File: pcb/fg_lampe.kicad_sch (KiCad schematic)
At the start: 42 parts, among them J1 ISP Port, J2 I^{2}C Debug, J3 RX/TX, J4 1792863, J5 1792863, J6 1792863, SW1 Reset Button, U1 ATmega328P-P, U2 L7805, U3 MAX1044, U4 MAX1044, U5 MCP4812, U8 MCP3008, Y1 16MHz

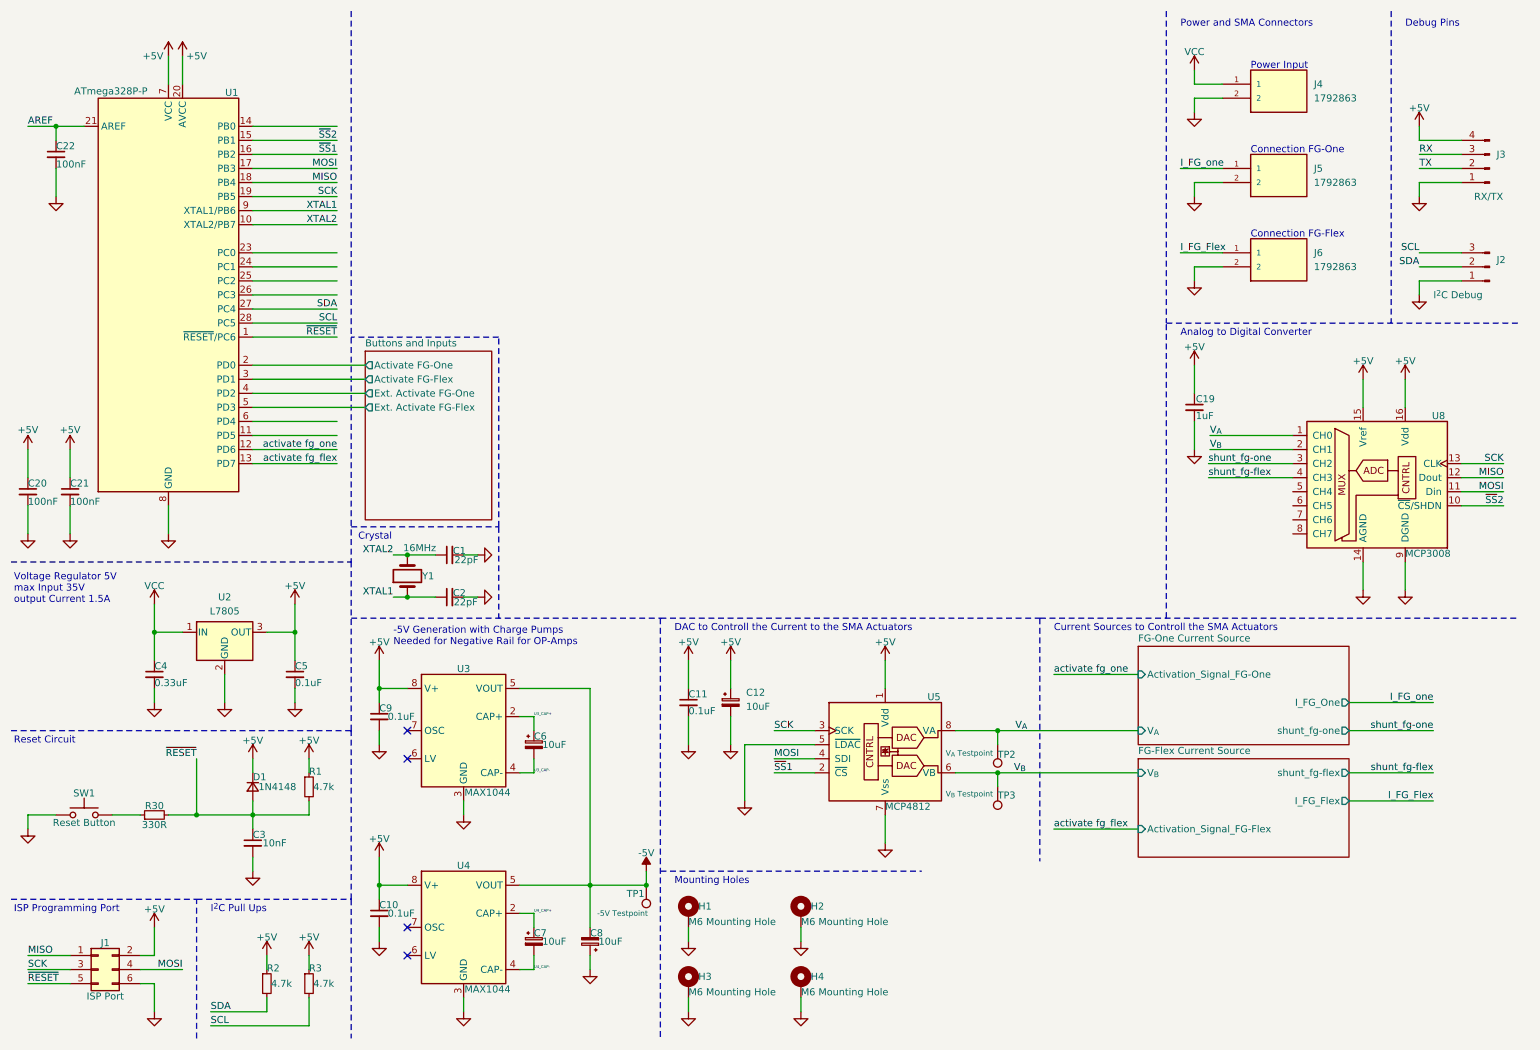
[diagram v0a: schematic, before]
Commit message: potentiometer to set pwm for warm and cold light added
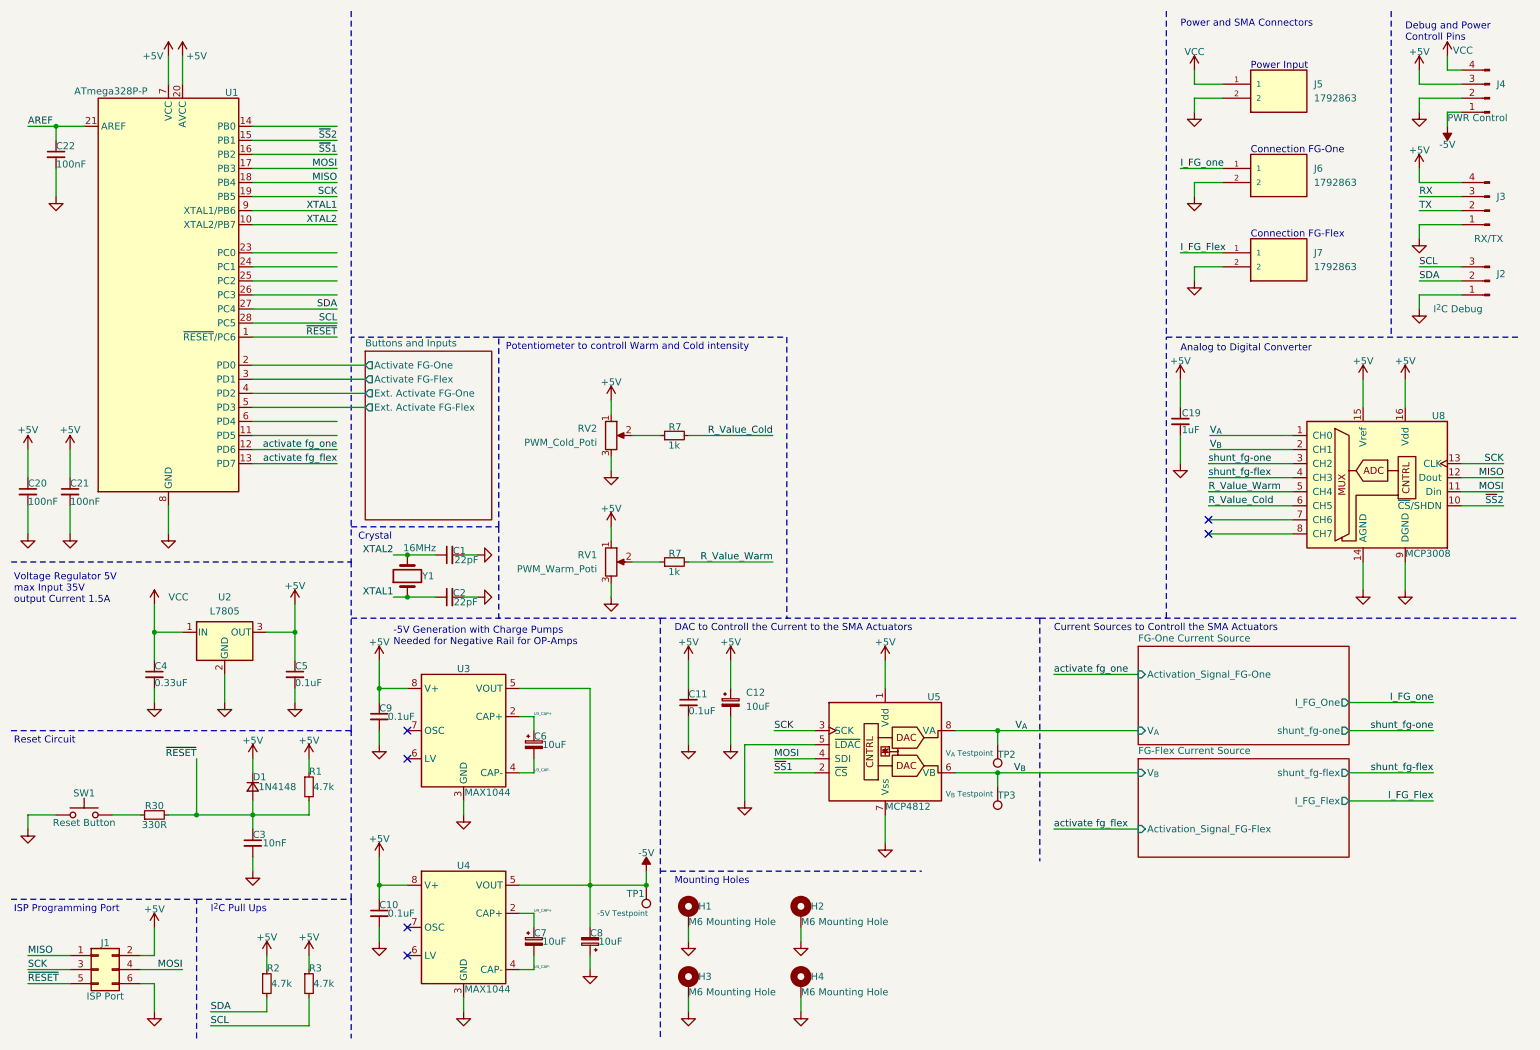
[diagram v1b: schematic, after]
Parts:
- added J4: PWR Control, Connector_PinHeader_2.54mm:PinHeader_1x04_P2.54mm_Vertical, symbol Connector:Conn_01x04_Pin
- added R7 (x2): 1k, Resistor_THT:R_Axial_DIN0207_L6.3mm_D2.5mm_P10.16mm_Horizontal, symbol Device:R_Small
- added RV1: PWM_Warm_Poti, symbol Device:R_Potentiometer
- added RV2: PWM_Cold_Poti, symbol Device:R_Potentiometer
- renumbered J4 to J5, J5 to J6, J6 to J7
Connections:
- net +5V: now also J4.3 (Pin_3), RV1.1, RV2.1
- net -5V: now also J4.1 (Pin_1)
- net GND: now also J4.2 (Pin_2), RV1.3, RV2.3
- net VCC: now also J4.4 (Pin_4)
- net R_Value_Warm: now reaches U8.5 (CH4)
- net R_Value_Warm: now also R7.2
- net R_Value_Cold: now reaches U8.6 (CH5)
- net R_Value_Cold: now also R7.2
- new net: R7.1, RV1.2
- new net: R7.1, RV2.2
- no-connect marks 4 -> 6
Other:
- note added: "Debug and Power Controll Pins"
- note added: "Potentiometer to controll Warm and Cold intensity"
- note removed: "Debug Pins"
- title: Microcontroller und Peripherie -> Microcontroller and periferals
- moved on the sheet: C19, J2, J3

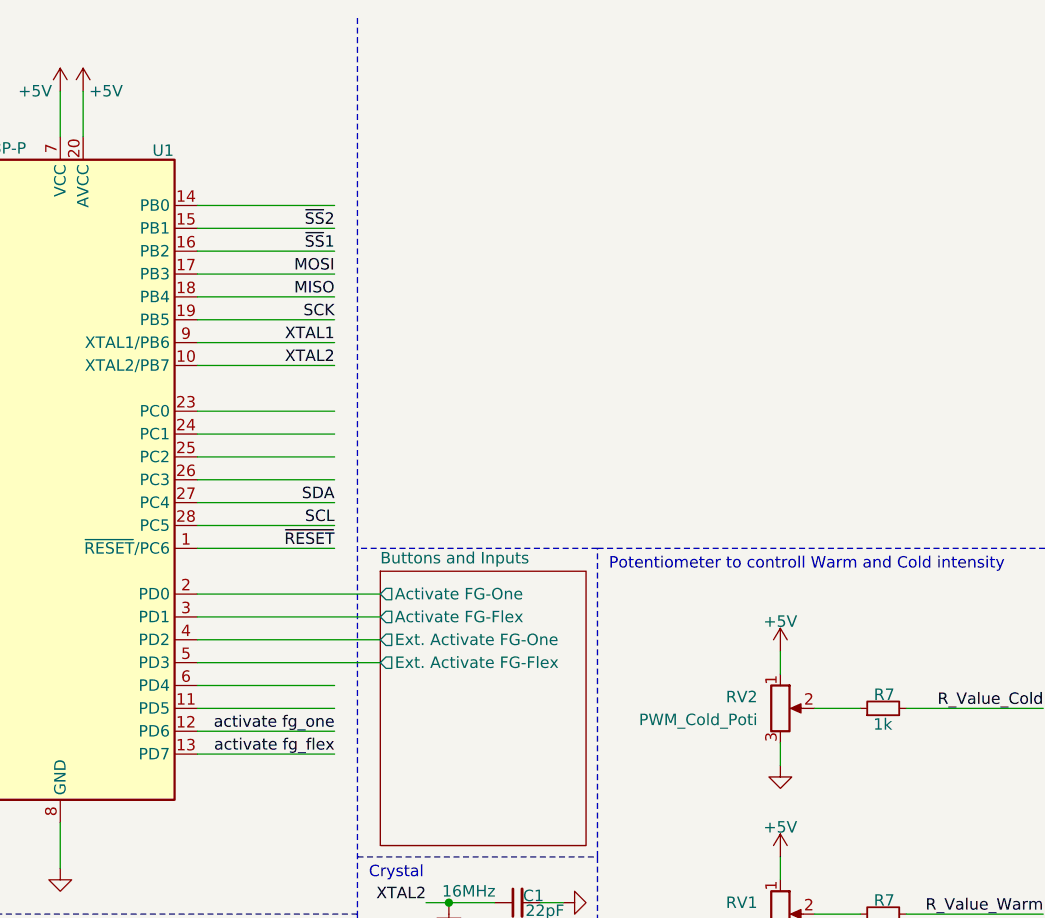
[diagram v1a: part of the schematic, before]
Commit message: gate driver added
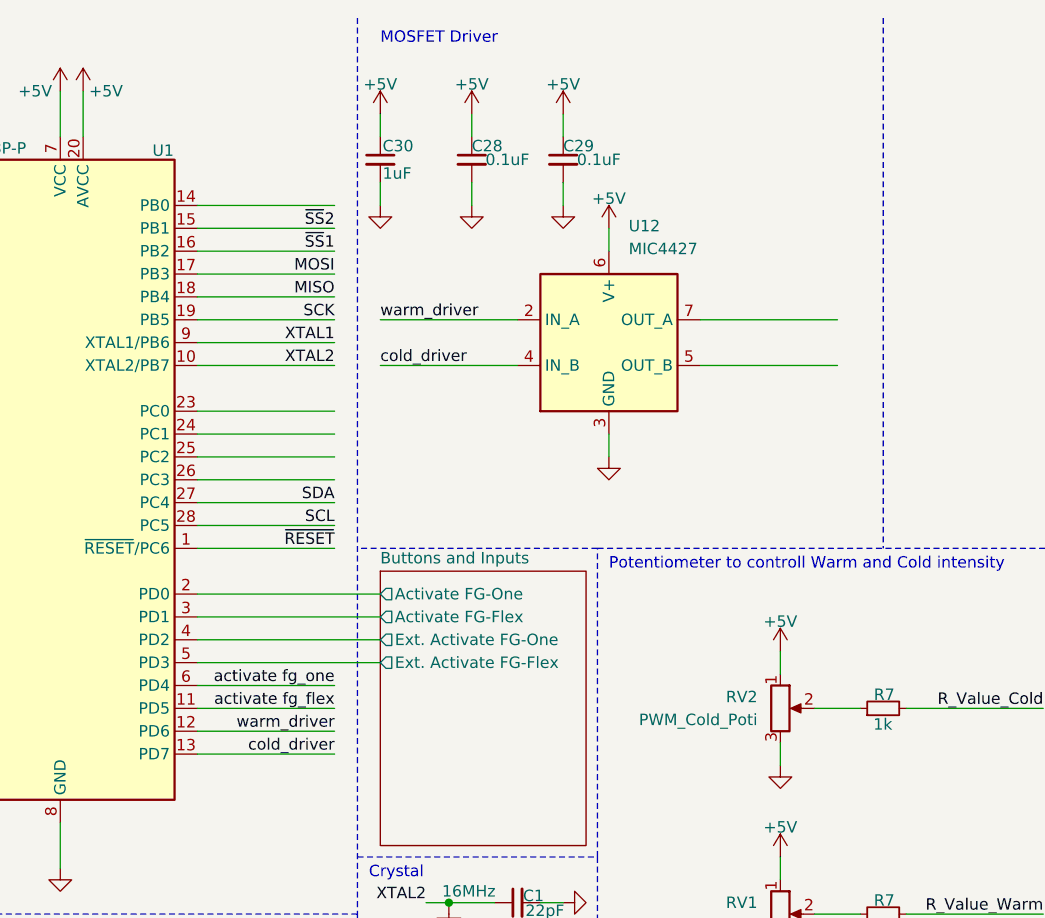
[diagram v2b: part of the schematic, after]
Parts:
- added C28, C29: 0.1uF, Capacitor_THT:C_Disc_D5.1mm_W3.2mm_P5.00mm, symbol Device:C_Small
- added C30: 1uF, Capacitor_THT:C_Disc_D4.7mm_W2.5mm_P5.00mm, symbol Device:C_Small
- added U12: MIC4427, symbol Driver_FET:MIC4427
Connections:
- net +5V: now also C28.1, C29.1, C30.1, U12.6 (V+)
- net GND: now also C28.2, C29.2, C30.2, U12.3 (GND)
- net activate fg_flex: now also U1.11 (PD5); no longer U1.13 (PD7)
- net activate fg_one: now also U1.6 (PD4); no longer U1.12 (PD6)
- new net cold_driver: U1.13 (PD7), U12.4 (IN_B)
- new net warm_driver: U1.12 (PD6), U12.2 (IN_A)
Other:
- note added: "MOSFET Driver"

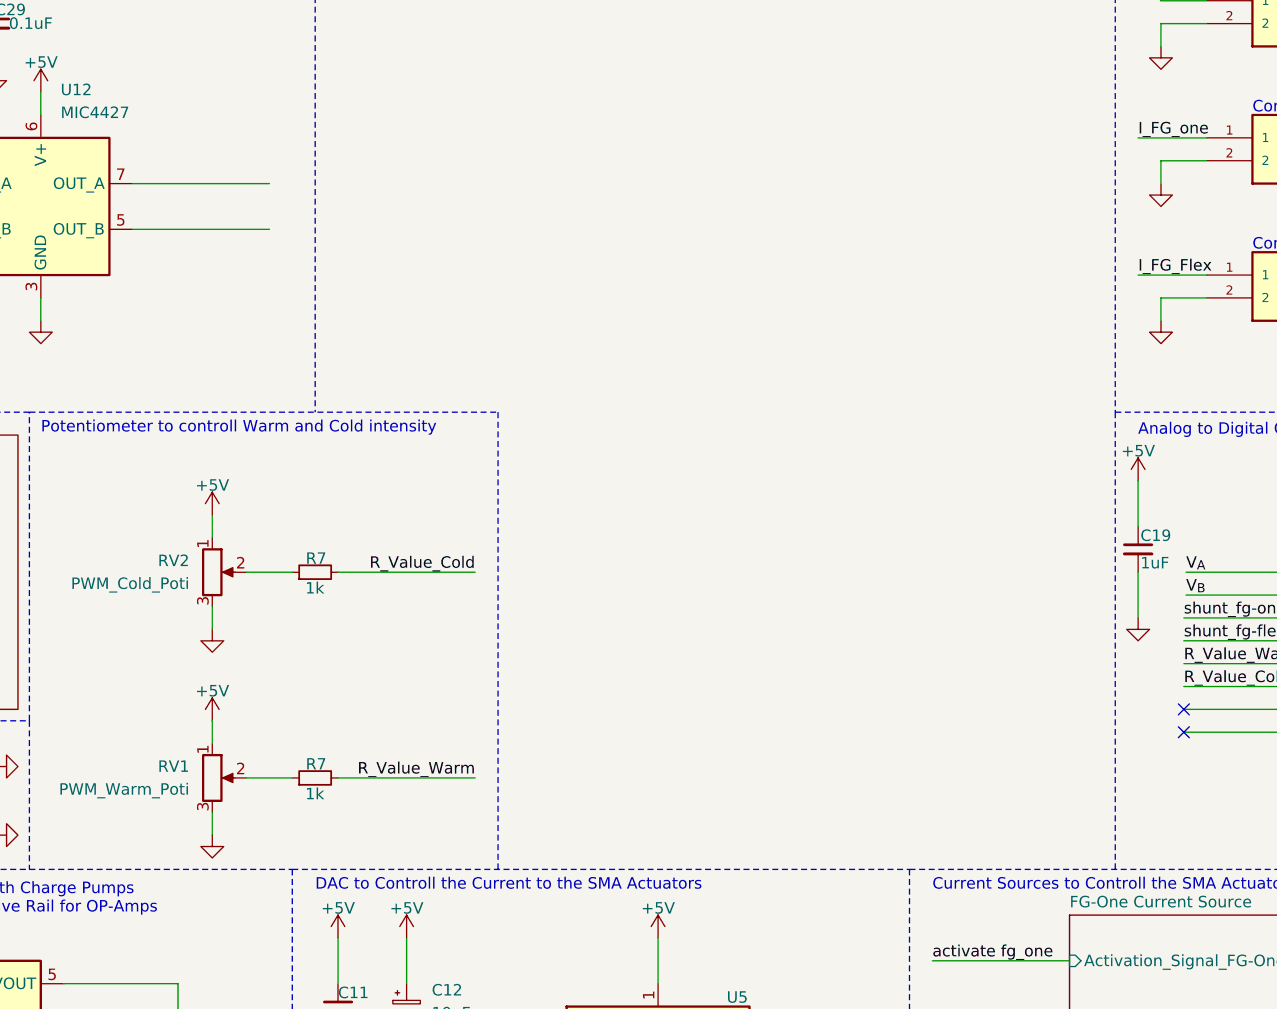
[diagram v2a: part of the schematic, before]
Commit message: mosfet for LEDs added
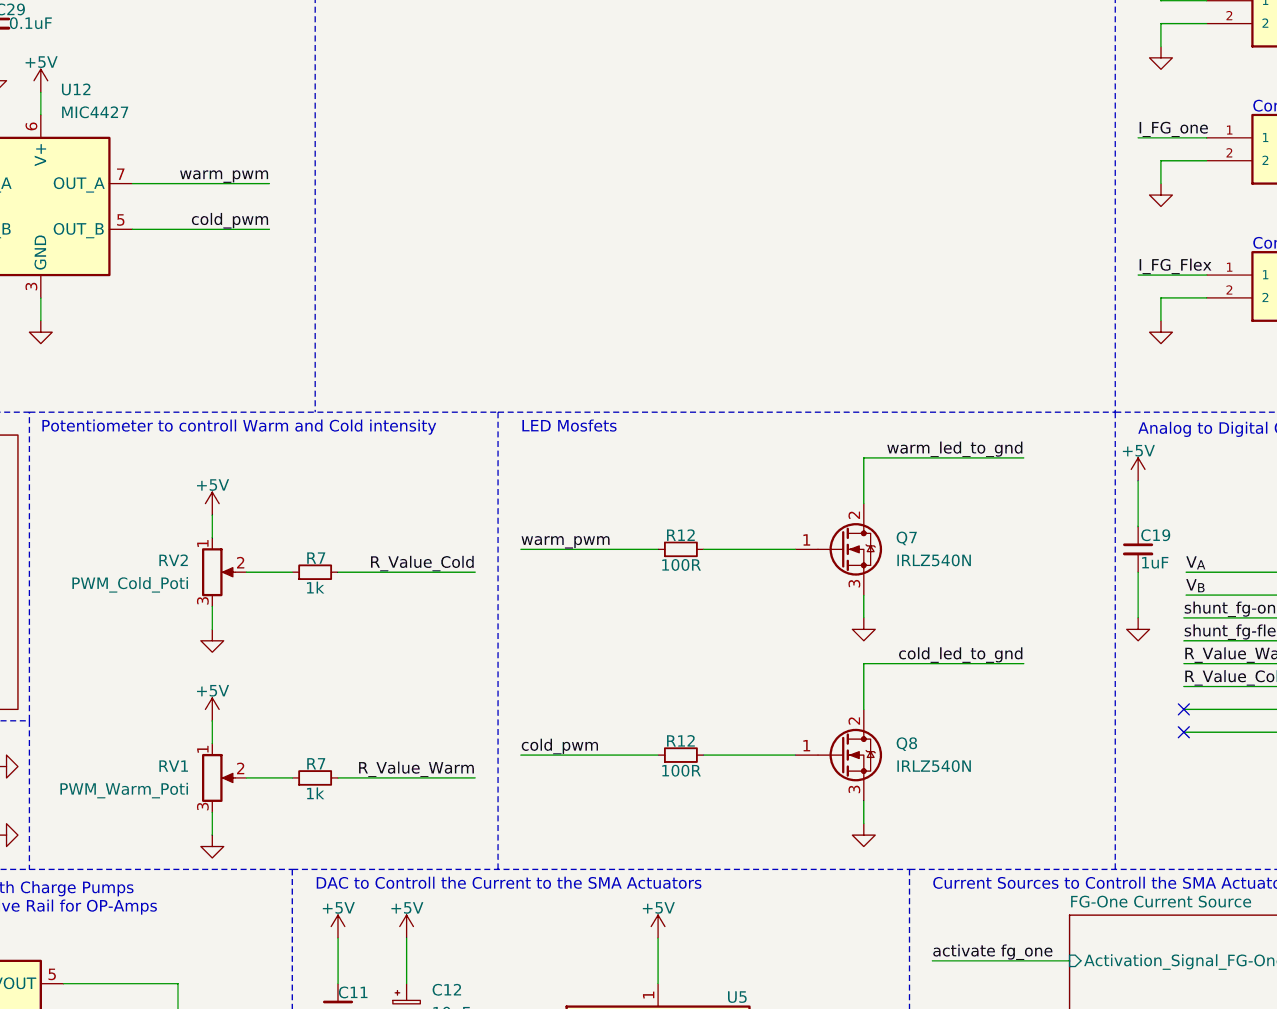
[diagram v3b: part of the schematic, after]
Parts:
- added Q7, Q8: IRLZ540N, Package_TO_SOT_THT:TO-220-3_Horizontal_TabDown, symbol Transistor_FET:IRLZ34N
- added R12 (x2): 100R, Resistor_THT:R_Axial_DIN0207_L6.3mm_D2.5mm_P10.16mm_Horizontal, symbol Device:R_Small
- U12: footprint (none) -> Package_DIP:DIP-8_W7.62mm_Socket_LongPads
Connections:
- net GND: now also Q7.3 (S), Q8.3 (S)
- net cold_pwm: now reaches U12.5 (OUT_B)
- net cold_pwm: now also R12.1
- net warm_pwm: now reaches U12.7 (OUT_A)
- net warm_pwm: now also R12.1
- new net: Q8.1 (G), R12.2
- new net: Q7.1 (G), R12.2
- new net cold_led_to_gnd: Q8.2 (D)
- new net warm_led_to_gnd: Q7.2 (D)
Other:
- note added: "LED Mosfets"
